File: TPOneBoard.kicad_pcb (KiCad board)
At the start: 2 copper layers, 100.5 x 45 mm, 31 parts, among them J1 BME/BMP280, J2 BH 1750 FVI, J3 Conn_01x06_Pin, J4 TP4056 Modul, J6 Conn_01x01_Pin, J7 Screw_Terminal_01x02, Q1 UMH3N, SW2 Reset, SW3 Close for prog., U1 MCP1700-3302E, U6 ESP-07S

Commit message: 1. Stufe
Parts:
- removed BT1: Battery_Cell, Battery:BatteryHolder_MPD_BH-18650-PC2
- removed C1, C2: 100nf, FootPrints_TPC:C_1206_HandSolder
- removed C3: 100uf, Capacitor_THT:CP_Radial_D6.3mm_P2.50mm
- removed D1, D2, D3: LED, FootPrints_TPC:LED_1206_3216_TPC_Metric_Pad1.42x1.75mm_HandSolder
- removed JP15: Deep Sleep, Jumper:SolderJumper-2_P1.3mm_Bridged_RoundedPad1.0x1.5mm
- removed JP5: Reset, Connector_PinHeader_2.54mm:PinHeader_1x02_P2.54mm_Vertical
- removed Q1: UMH3N, Package_TO_SOT_SMD:SOT-363_SC-70-6
- removed SW2: Reset, FootPrints_TPC:SW_TH_Tactile_Omron
- removed SW3: Close for prog., FootPrints_TPC:SW_TH_Tactile_Omron
- removed U6: ESP-07S, RF_Module:ESP-07
- added BT2: Battery_Cell, Battery:BatteryHolder_MPD_BH-18650-PC2, B.Cu at (168.1, 95.6)
- added C4: 100nf, FootPrints_TPC:C_1206_HandSolder, F.Cu at (197.2, 86.4)
- added C5: 100uf, Capacitor_THT:CP_Radial_D6.3mm_P2.50mm, F.Cu at (149.4, 119.7)
- added C6: 100nf, FootPrints_TPC:C_1206_HandSolder, F.Cu at (150.9, 113.0)
- added D4: LED, FootPrints_TPC:LED_1206_3216_TPC_Metric_Pad1.42x1.75mm_HandSolder, F.Cu at (187.5, 117.9)
- added J5: TP4056 Modul, FootPrints_TPC:TP4056-18650, F.Cu at (163.7, 82.3)
- added J8: Conn_01x04_Socket, Connector_PinSocket_2.54mm:PinSocket_1x04_P2.54mm_Vertical, B.Cu at (227.1, 99.3)
- added JP2: Reset, Connector_PinHeader_2.54mm:PinHeader_1x02_P2.54mm_Vertical, F.Cu at (181.0, 84.9)
- added JP6: 3.3V Off, Connector_PinHeader_2.54mm:PinHeader_1x02_P2.54mm_Vertical, F.Cu at (168.9, 84.9)
- added Q2: UMH3N, Package_TO_SOT_SMD:SOT-363_SC-70-6, F.Cu at (210.1, 85.5)
- added SW4: Close for prog., FootPrints_TPC:SW_TH_Tactile_Omron, F.Cu at (234.8, 84.1)
- added SW5: Reset, FootPrints_TPC:SW_TH_Tactile_Omron, F.Cu at (186.5, 84.1)
- added U2: MCP1700x-330xxTO, Package_TO_SOT_THT:TO-92L_Inline_Wide, F.Cu at (159.5, 120.9)
- added U7: ESP-07S, RF_Module:ESP-07, F.Cu at (202.1, 114.5)
- J1: value BME/BMP280 -> BH 1750 FVI; footprint Connector_PinSocket_2.54mm:PinSocket_1x04_P2.54mm_Vertical -> Connector_JST:JST_XH_B5B-XH-A_1x05_P2.50mm_Vertical; moved to F.Cu
- J2: value BH 1750 FVI -> BME/BMP280; footprint Connector_JST:JST_XH_B5B-XH-A_1x05_P2.50mm_Vertical -> Connector_PinSocket_2.54mm:PinSocket_1x04_P2.54mm_Vertical; moved to B.Cu
- J4: value TP4056 Modul -> Conn_01x02_Pin; footprint FootPrints_TPC:TP4056-18650 -> Connector_PinHeader_2.54mm:PinHeader_1x02_P2.54mm_Vertical
- J6: value Conn_01x01_Pin -> Screw_Terminal_01x02; footprint Connector_PinSocket_2.54mm:PinSocket_1x01_P2.54mm_Vertical -> WAGO:WAGO_250_202_1x2_TPC; moved to B.Cu
- J7: value Screw_Terminal_01x02 -> Conn_01x04_Socket; footprint WAGO:WAGO_250_202_1x2_TPC -> Connector_PinSocket_2.54mm:PinSocket_1x04_P2.54mm_Vertical
- JP1: value 3.3V -> Deep Sleep; footprint Connector_PinHeader_2.54mm:PinHeader_1x02_P2.54mm_Vertical -> Jumper:SolderJumper-2_P1.3mm_Bridged_RoundedPad1.0x1.5mm
- JP3: value RTS CTS -> 3.3V; footprint Jumper:SolderJumper-2_P1.3mm_Open_RoundedPad1.0x1.5mm -> Connector_PinHeader_2.54mm:PinHeader_1x02_P2.54mm_Vertical
- R1: value 2K -> 47K
- R2: value 2K -> 12k
- R3: value 2K -> 180K
- R4: value 120K -> 56K; footprint Resistor_THT:R_Axial_DIN0207_L6.3mm_D2.5mm_P7.62mm_Horizontal -> FootPrints_TPC:R_1206_HandSolder
- R5: value 56K -> 2K; footprint Resistor_THT:R_Axial_DIN0207_L6.3mm_D2.5mm_P7.62mm_Horizontal -> FootPrints_TPC:R_1206_HandSolder
- U1: value MCP1700-3302E -> CD4051B; footprint Package_TO_SOT_THT:TO-92L_Inline_Wide -> Package_SO:SSOP-16_4.4x5.2mm_P0.65mm
- moved J1 69.4 mm to (238.6, 111.4), turned to -90 degrees
- moved J6 61.6 mm to (164.6, 114.0), turned to 90 degrees
- moved J2 61.3 mm to (176.5, 118.7), turned to 0 degrees
- moved JP3 37.4 mm to (175.1, 87.6), turned to 180 degrees
- moved R9 36.9 mm to (217.8, 112.1), turned to 0 degrees
- moved R5 34.9 mm to (187.6, 113.1), turned to 180 degrees
- moved J4 33.3 mm to (203.8, 87.6)
- moved U1 32.8 mm to (187.3, 106.4)
- moved R6 30.2 mm to (188.7, 100.0), turned to 180 degrees
- moved R4 23.2 mm to (167.1, 105.5), turned to 180 degrees
- moved R3 22.2 mm to (167.1, 102.7), turned to 0 degrees
- moved JP1 11.7 mm to (202.3, 109.9), turned to 0 degrees
- moved J7 11.2 mm to (155.9, 99.4), turned to 0 degrees
- moved R2 10.7 mm to (178.1, 102.7)
- moved J3 5.13 mm to (195.4, 99.9)
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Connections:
- J1 pad 1: +3.3V -> unconnected-(J1-Pin_1-Pad1)
- J1 pad 3: SCL -> SDA
- J1 pad 4: SDA -> SCL
- J2 pad 1: unconnected-(J2-Pin_1-Pad1) -> +3.3V
- J2 pad 3: SDA -> SCL
- J2 pad 4: SCL -> SDA
- J3 pad 5: Net-(J3-Pin_5) -> unconnected-(J3-Pin_5-Pad5)
- J4 pad 1: SCell+ -> DTR
- J4 pad 2: SCell- -> RTS
- J6 pad 1: RTS -> SCell+
- J7 pad 1: SCell+ -> 18650+
- J7 pad 2: SCell- -> 18650-
- JP1 pad 1: +3.3V -> RST
- JP1 pad 2: Net-(J3-Pin_4) -> DeepS
- JP3 pad 1: RTS -> +3.3V
- JP3 pad 2: Net-(J3-Pin_5) -> Net-(J3-Pin_4)
- R1 pad 1: Net-(D1-A) -> SCell+
- R1 pad 2: +3.3V -> SolarPanel
- R2 pad 1: Net-(D2-A) -> SolarPanel
- R2 pad 2: +3.3V -> GND
- R3 pad 1: Net-(D3-A) -> 18650+
- R3 pad 2: +3.3V -> Akku
- R4 pad 1: 18650+ -> Akku
- R4 pad 2: ADC -> GND
- R5 pad 1: ADC -> Net-(D4-A)
- R5 pad 2: GND -> +3.3V
- U1 pad 2: 4056 Out+ -> GND
- U1 pad 3: +3.3V -> ADC
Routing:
- net ADC: track 126.0 -> 0.00 mm, vias 1 -> 0
- net 18650+: track 24.2 -> 129.4 mm
- net RST: track 110.2 -> 13.6 mm, vias 1 -> 0
- net +3.3V: track 153.3 -> 66.7 mm, vias 0 -> 1
- net SDA: track 71.4 -> 0.00 mm, vias 1 -> 0
- net SCL: track 70.7 -> 0.00 mm, vias 1 -> 0
- net Net-(JP6-B): track 0.00 -> 58.6 mm, vias 0 -> 1
- net IO0: track 55.1 -> 0.50 mm, vias 2 -> 0
- net GND: track 34.6 -> 0.00 mm, vias 2 -> 0
- net Net-(J3-Pin_4): track 5.67 -> 39.9 mm, vias 0 -> 1
- net RTS: track 31.1 -> 0.00 mm
- net TXD: track 30.0 -> 0.00 mm
- net Akku: track 0.00 -> 28.5 mm
- net Net-(U7-GPIO15): track 25.9 -> 0.00 mm, vias 2 -> 0
- net RXD: track 24.5 -> 0.00 mm
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- added copper zone on F.Cu, net GND
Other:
- board text added: "82,75"
- board text removed: "3.3"
- board text removed: "ADC"
- board text removed: "Antenne"
- board text removed: "EN"
- board text removed: "GPO15"
- board text removed: "IO0"
- board text removed: "IO12"
- board text removed: "IO13"
- board text removed: "IO14"
- board text removed: "IO16"
- board text removed: "LED"
- board text removed: "RST"
- board text removed: "RXD"
- board text removed: "TXD"
- board text removed: "X"

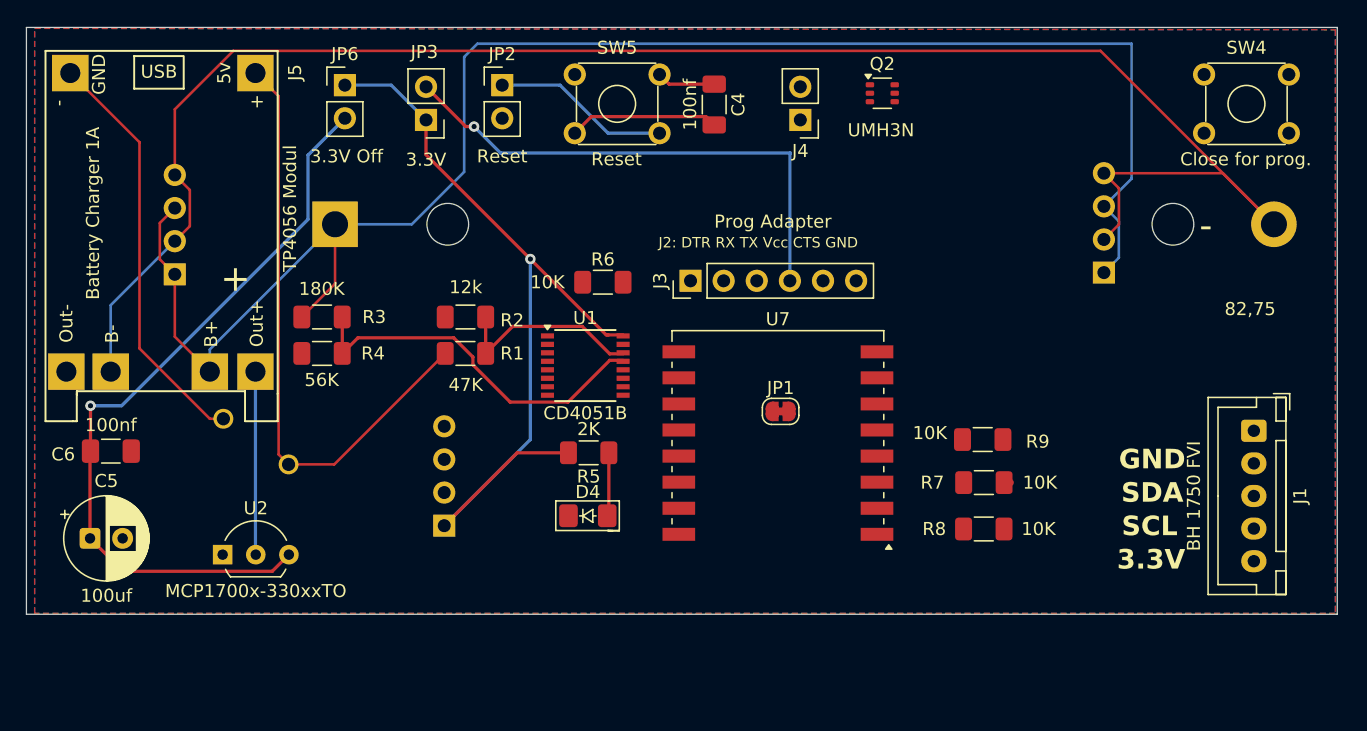
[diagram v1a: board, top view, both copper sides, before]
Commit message: Platine Bestellt am 30.07.2025 Signed-off-by: TPComputerservice <78719315+TPComputerservice@users.noreply.github.com>
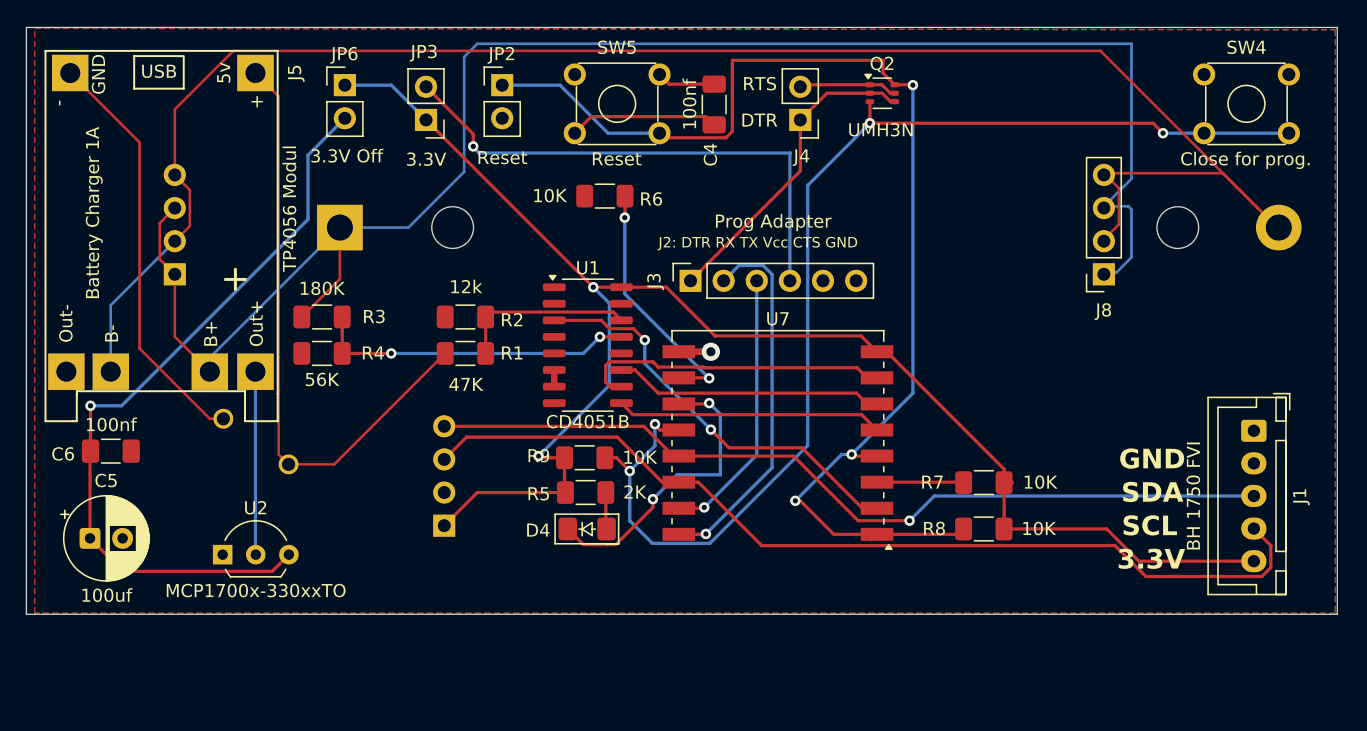
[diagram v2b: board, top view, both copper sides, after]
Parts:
- removed JP1: Deep Sleep, Jumper:SolderJumper-2_P1.3mm_Bridged_RoundedPad1.0x1.5mm
- added G***: LOGO, FootPrints_TPC:TPC_Logo, B.Cu at (225.7, 112.1)
- J3: footprint Connector_PinHeader_2.54mm:PinHeader_1x06_P2.54mm_Vertical -> Connector_PinSocket_2.54mm:PinSocket_1x06_P2.54mm_Vertical
- J8: moved to F.Cu
- U1: footprint Package_SO:SSOP-16_4.4x5.2mm_P0.65mm -> Package_SO:SO-16_3.9x9.9mm_P1.27mm
- moved R9 30.6 mm to (187.3, 113.5), turned to 180 degrees
- moved R6 6.61 mm to (188.8, 93.4)
- moved R5 3.05 mm to (187.4, 116.2)
- moved U1 1.58 mm to (187.5, 104.9)
- moved D4 1.02 mm to (187.5, 118.9)
- moved BT2 0.45 mm to (168.5, 95.8)
- moved J8 0.13 mm to (227.1, 99.4), turned to 180 degrees
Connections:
- JP2 pad 1: RST -> DeepS
- Q2 pad 6: RST -> DeepS
- R8 pad 1: RST -> DeepS
- SW5 pad 4: RST -> DeepS
- U1 pad 1: GND -> unconnected-(U1-X4-Pad1)
- U1 pad 12: GND -> unconnected-(U1-X3-Pad12)
- U1 pad 15: GND -> unconnected-(U1-X2-Pad15)
- U1 pad 2: GND -> unconnected-(U1-X6-Pad2)
- U1 pad 4: GND -> unconnected-(U1-X7-Pad4)
- U1 pad 5: GND -> unconnected-(U1-X5-Pad5)
- U7 pad 1: RST -> DeepS
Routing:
- net DeepS: track 0.00 -> 93.1 mm, vias 0 -> 3
- net IO0: track 0.50 -> 91.0 mm, vias 0 -> 4
- net SCL: track 0.00 -> 72.3 mm
- net SDA: track 0.00 -> 65.9 mm, vias 0 -> 1
- net +3.3V: track 66.7 -> 119.2 mm, vias 1 -> 2
- net ADC: track 0.00 -> 31.9 mm, vias 0 -> 2
- net TXD: track 0.00 -> 28.6 mm, vias 0 -> 1
- net DTR: track 0.00 -> 24.2 mm
- net IO13: track 0.00 -> 24.1 mm
- net LED_Buildin: track 0.00 -> 23.0 mm, vias 0 -> 2
- net IO14: track 0.00 -> 21.5 mm
- net RXD: track 0.00 -> 21.0 mm, vias 0 -> 1
- net IO12: track 0.00 -> 20.7 mm
- net Net-(U7-GPIO15): track 0.00 -> 19.0 mm, vias 0 -> 2
- net RST: track 13.6 -> 0.00 mm
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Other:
- board text added: "18650 - 18650 + 18650 - 18650 +"
- board text added: "DTR"
- board text added: "RTS"
- board text added: "SDA SCL GND 3.3V"
- board text added: "TP Computerservice Ditzingen ONE Board V3.0"
- board text removed: "82,75"
